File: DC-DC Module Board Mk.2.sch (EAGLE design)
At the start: 151 parts, among them Q1 FDN340P, U2 AP1117_LIN_REG, U3 LM1085IS-5.0

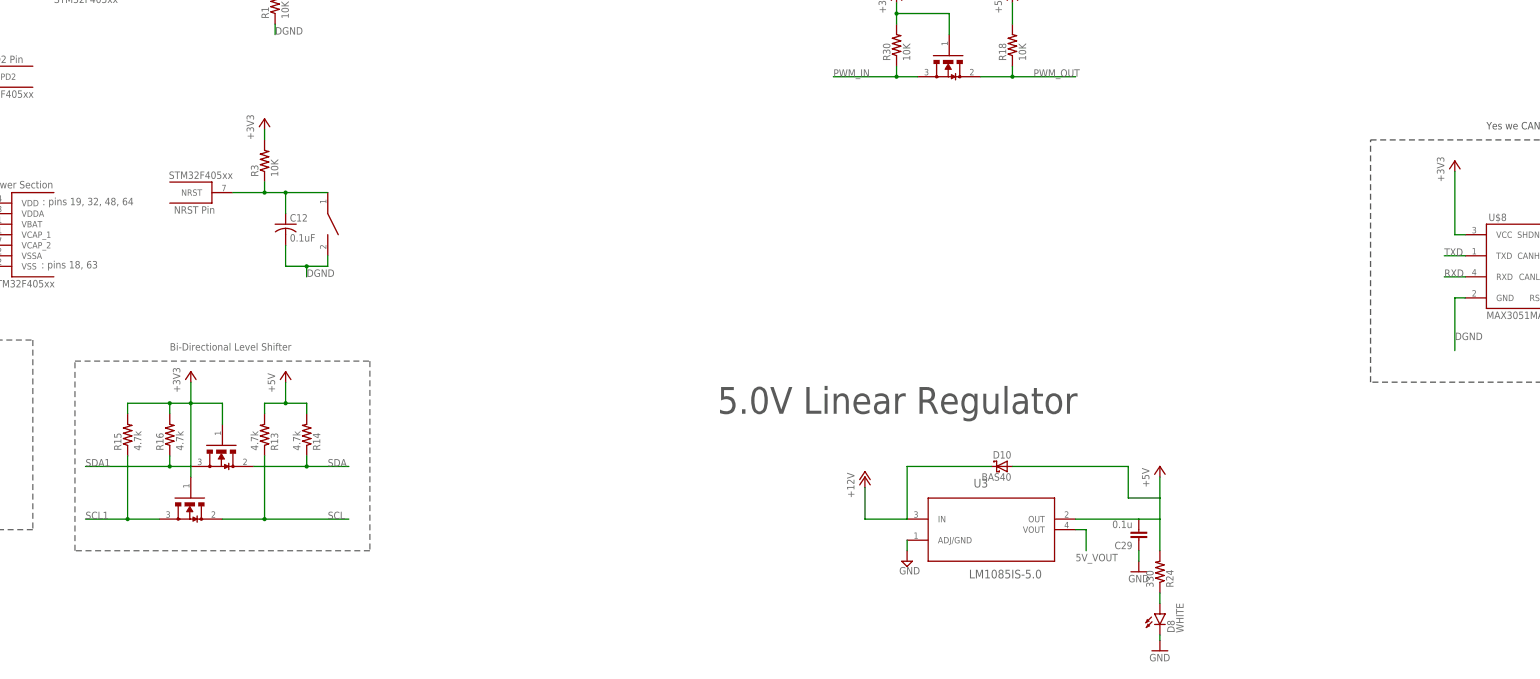
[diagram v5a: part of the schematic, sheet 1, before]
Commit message: Added header pins for debugging
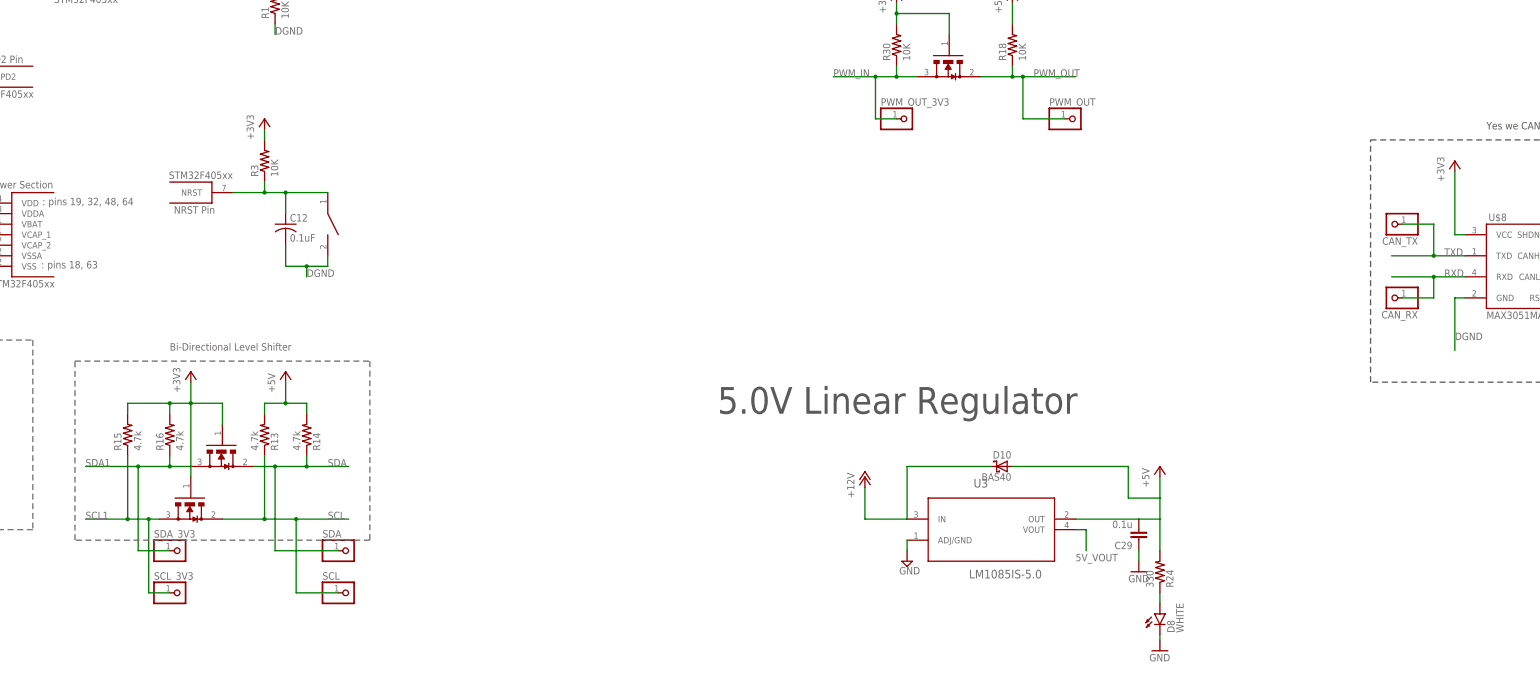
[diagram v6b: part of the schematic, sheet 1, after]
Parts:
- added CAN_RX, CAN_TX, PWM_OUT, PWM_OUT_3V3, SCL, SCL_3V3, SDA, SDA_3V3: (no value), pinhead:PINHD-1X1
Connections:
- net PWM_IN: now also PWM_OUT_3V3.1
- net PWM_OUT: now also PWM_OUT.1
- net RXD: now also CAN_RX.1
- net SCL: now also SCL.1
- net SCL1: now also SCL_3V3.1
- net SDA: now also SDA.1
- net SDA1: now also SDA_3V3.1
- net TXD: now also CAN_TX.1
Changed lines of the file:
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@@
 <?xml version="1.0" encoding="utf-8"?>
 <!DOCTYPE eagle SYSTEM "eagle.dtd">
-<eagle version="7.4.0">
+<eagle version="7.5.0">
 <drawing>
 <settings>
@@
 <part name="+3V7" library="supply1" deviceset="+3V3" device=""/>
 <part name="P+1" library="supply1" deviceset="+5V" device=""/>
+<part name="PWM_OUT_3V3" library="pinhead" deviceset="PINHD-1X1" device=""/>
+<part name="PWM_OUT" library="pinhead" deviceset="PINHD-1X1" device=""/>
+<part name="SDA_3V3" library="pinhead" deviceset="PINHD-1X1" device=""/>
+<part name="SCL_3V3" library="pinhead" deviceset="PINHD-1X1" device=""/>
+<part name="SDA" library="pinhead" deviceset="PINHD-1X1" device=""/>
+<part name="SCL" library="pinhead" deviceset="PINHD-1X1" device=""/>
+<part name="CAN_TX" library="pinhead" deviceset="PINHD-1X1" device=""/>
+<part name="CAN_RX" library="pinhead" deviceset="PINHD-1X1" device=""/>
 </parts>
 <sheets>
@@
 <wire x1="459.74" y1="-127" x2="459.74" y2="-68.58" width="0.1524" layer="97" style="shortdash"/>
 <text x="487.68" y="-66.04" size="1.778" layer="97">Yes we CAN!</text>
-<wire x1="218.44" y1="-167.64" x2="147.32" y2="-167.64" width="0.1524" layer="95" style="shortdash"/>
-<wire x1="147.32" y1="-167.64" x2="147.32" y2="-121.92" width="0.1524" layer="95" style="shortdash"/>
+<wire x1="218.44" y1="-165.1" x2="147.32" y2="-165.1" width="0.1524" layer="95" style="shortdash"/>
+<wire x1="147.32" y1="-165.1" x2="147.32" y2="-121.92" width="0.1524" layer="95" style="shortdash"/>
 <wire x1="147.32" y1="-121.92" x2="218.44" y2="-121.92" width="0.1524" layer="95" style="shortdash"/>
-<wire x1="218.44" y1="-121.92" x2="218.44" y2="-167.64" width="0.1524" layer="95" style="shortdash"/>
+<wire x1="218.44" y1="-121.92" x2="218.44" y2="-165.1" width="0.1524" layer="95" style="shortdash"/>
 <text x="170.18" y="-119.38" size="1.778" layer="95">Bi-Directional Level Shifter</text>
 <text x="12.7" y="208.28" size="5.08" layer="97">Brick 1</text>
@@
 <instance part="+3V7" gate="G$1" x="345.44" y="-33.02"/>
 <instance part="P+1" gate="1" x="373.38" y="-33.02"/>
+<instance part="PWM_OUT_3V3" gate="G$1" x="347.98" y="-63.5"/>
+<instance part="PWM_OUT" gate="G$1" x="388.62" y="-63.5"/>
+<instance part="SDA_3V3" gate="G$1" x="172.72" y="-167.64"/>
+<instance part="SCL_3V3" gate="G$1" x="172.72" y="-177.8"/>
+<instance part="SDA" gate="G$1" x="213.36" y="-167.64"/>
+<instance part="SCL" gate="G$1" x="213.36" y="-177.8"/>
+<instance part="CAN_TX" gate="G$1" x="464.82" y="-88.9" rot="R180"/>
+<instance part="CAN_RX" gate="G$1" x="464.82" y="-106.68" rot="R180"/>
 </instances>
 <busses>
@@
 <wire x1="182.88" y1="-160.02" x2="193.04" y2="-160.02" width="0.1524" layer="91"/>
 <pinref part="R13" gate="G$1" pin="1"/>
-<wire x1="193.04" y1="-160.02" x2="213.36" y2="-160.02" width="0.1524" layer="91"/>
+<wire x1="193.04" y1="-160.02" x2="200.66" y2="-160.02" width="0.1524" layer="91"/>
+<wire x1="200.66" y1="-160.02" x2="213.36" y2="-160.02" width="0.1524" layer="91"/>
 <wire x1="193.04" y1="-144.78" x2="193.04" y2="-160.02" width="0.1524" layer="91"/>
 <junction x="193.04" y="-160.02"/>
 <label x="208.28" y="-160.02" size="1.778" layer="95"/>
+<pinref part="SCL" gate="G$1" pin="1"/>
+<wire x1="200.66" y1="-177.8" x2="210.82" y2="-177.8" width="0.1524" layer="91"/>
+<wire x1="200.66" y1="-177.8" x2="200.66" y2="-160.02" width="0.1524" layer="91"/>
+<junction x="200.66" y="-160.02"/>
 </segment>
 <segment>
@@
 <segment>
 <pinref part="U$9" gate="G$1" pin="D"/>
-<wire x1="190.5" y1="-147.32" x2="203.2" y2="-147.32" width="0.1524" layer="91"/>
+<wire x1="190.5" y1="-147.32" x2="195.58" y2="-147.32" width="0.1524" layer="91"/>
 <pinref part="R14" gate="G$1" pin="1"/>
+<wire x1="195.58" y1="-147.32" x2="203.2" y2="-147.32" width="0.1524" layer="91"/>
 <wire x1="203.2" y1="-147.32" x2="213.36" y2="-147.32" width="0.1524" layer="91"/>
 <wire x1="203.2" y1="-144.78" x2="203.2" y2="-147.32" width="0.1524" layer="91"/>
 <junction x="203.2" y="-147.32"/>
 <label x="208.28" y="-147.32" size="1.778" layer="95"/>
+<wire x1="195.58" y1="-147.32" x2="195.58" y2="-167.64" width="0.1524" layer="91"/>
+<junction x="195.58" y="-147.32"/>
+<pinref part="SDA" gate="G$1" pin="1"/>
+<wire x1="195.58" y1="-167.64" x2="210.82" y2="-167.64" width="0.1524" layer="91"/>
 </segment>
 <segment>
@@
 <segment>
 <pinref part="U$8" gate="G$1" pin="TXD"/>
-<wire x1="482.6" y1="-96.52" x2="477.52" y2="-96.52" width="0.1524" layer="91"/>
 <label x="477.52" y="-96.52" size="1.778" layer="95"/>
+<wire x1="482.6" y1="-96.52" x2="474.98" y2="-96.52" width="0.1524" layer="91"/>
+<wire x1="474.98" y1="-96.52" x2="464.82" y2="-96.52" width="0.1524" layer="91"/>
+<wire x1="474.98" y1="-96.52" x2="474.98" y2="-88.9" width="0.1524" layer="91"/>
+<junction x="474.98" y="-96.52"/>
+<pinref part="CAN_TX" gate="G$1" pin="1"/>
+<wire x1="474.98" y1="-88.9" x2="467.36" y2="-88.9" width="0.1524" layer="91"/>
 </segment>
 <segment>
@@
 <segment>
 <pinref part="U$8" gate="G$1" pin="RXD"/>
-<wire x1="482.6" y1="-101.6" x2="477.52" y2="-101.6" width="0.1524" layer="91"/>
 <label x="477.52" y="-101.6" size="1.778" layer="95"/>
+<wire x1="482.6" y1="-101.6" x2="474.98" y2="-101.6" width="0.1524" layer="91"/>
+<wire x1="474.98" y1="-101.6" x2="464.82" y2="-101.6" width="0.1524" layer="91"/>
+<wire x1="474.98" y1="-101.6" x2="474.98" y2="-106.68" width="0.1524" layer="91"/>
+<junction x="474.98" y="-101.6"/>
+<pinref part="CAN_RX" gate="G$1" pin="1"/>
+<wire x1="474.98" y1="-106.68" x2="467.36" y2="-106.68" width="0.1524" layer="91"/>
 </segment>
 <segment>
@@
 <wire x1="175.26" y1="-147.32" x2="170.18" y2="-147.32" width="0.1524" layer="91"/>
 <pinref part="R16" gate="G$1" pin="1"/>
-<wire x1="170.18" y1="-147.32" x2="149.86" y2="-147.32" width="0.1524" layer="91"/>
+<wire x1="170.18" y1="-147.32" x2="162.56" y2="-147.32" width="0.1524" layer="91"/>
+<wire x1="162.56" y1="-147.32" x2="149.86" y2="-147.32" width="0.1524" layer="91"/>
 <wire x1="170.18" y1="-147.32" x2="170.18" y2="-144.78" width="0.1524" layer="91"/>
 <junction x="170.18" y="-147.32"/>
 <label x="149.86" y="-147.32" size="1.778" layer="95"/>
+<wire x1="162.56" y1="-147.32" x2="162.56" y2="-167.64" width="0.1524" layer="91"/>
+<junction x="162.56" y="-147.32"/>
+<pinref part="SDA_3V3" gate="G$1" pin="1"/>
+<wire x1="162.56" y1="-167.64" x2="170.18" y2="-167.64" width="0.1524" layer="91"/>
 </segment>
 <segment>
@@
 <segment>
 <pinref part="BSS138" gate="G$1" pin="S"/>
-<wire x1="167.64" y1="-160.02" x2="160.02" y2="-160.02" width="0.1524" layer="91"/>
+<wire x1="167.64" y1="-160.02" x2="165.1" y2="-160.02" width="0.1524" layer="91"/>
 <pinref part="R15" gate="G$1" pin="1"/>
+<wire x1="165.1" y1="-160.02" x2="160.02" y2="-160.02" width="0.1524" layer="91"/>
 <wire x1="160.02" y1="-160.02" x2="149.86" y2="-160.02" width="0.1524" layer="91"/>
 <wire x1="160.02" y1="-144.78" x2="160.02" y2="-160.02" width="0.1524" layer="91"/>
 <junction x="160.02" y="-160.02"/>
 <label x="149.86" y="-160.02" size="1.778" layer="95"/>
+<wire x1="165.1" y1="-160.02" x2="165.1" y2="-177.8" width="0.1524" layer="91"/>
+<junction x="165.1" y="-160.02"/>
+<pinref part="SCL_3V3" gate="G$1" pin="1"/>
+<wire x1="165.1" y1="-177.8" x2="170.18" y2="-177.8" width="0.1524" layer="91"/>
 </segment>
 <segment>
@@
 <segment>
 <pinref part="R18" gate="G$1" pin="1"/>
-<wire x1="373.38" y1="-53.34" x2="388.62" y2="-53.34" width="0.1524" layer="91"/>
+<wire x1="373.38" y1="-53.34" x2="375.92" y2="-53.34" width="0.1524" layer="91"/>
+<wire x1="375.92" y1="-53.34" x2="388.62" y2="-53.34" width="0.1524" layer="91"/>
 <wire x1="373.38" y1="-50.8" x2="373.38" y2="-53.34" width="0.1524" layer="91"/>
 <pinref part="U$12" gate="G$1" pin="D"/>
@@
 <junction x="373.38" y="-53.34"/>
 <label x="378.46" y="-53.34" size="1.778" layer="95"/>
+<wire x1="375.92" y1="-53.34" x2="375.92" y2="-63.5" width="0.1524" layer="91"/>
+<junction x="375.92" y="-53.34"/>
+<pinref part="PWM_OUT" gate="G$1" pin="1"/>
+<wire x1="375.92" y1="-63.5" x2="386.08" y2="-63.5" width="0.1524" layer="91"/>
 </segment>
 <segment>
@@
 <pinref part="U$12" gate="G$1" pin="S"/>
 <pinref part="R30" gate="G$1" pin="1"/>
-<wire x1="345.44" y1="-53.34" x2="330.2" y2="-53.34" width="0.1524" layer="91"/>
+<wire x1="345.44" y1="-53.34" x2="340.36" y2="-53.34" width="0.1524" layer="91"/>
+<wire x1="340.36" y1="-53.34" x2="330.2" y2="-53.34" width="0.1524" layer="91"/>
 <wire x1="345.44" y1="-50.8" x2="345.44" y2="-53.34" width="0.1524" layer="91"/>
 <junction x="345.44" y="-53.34"/>
 <label x="330.2" y="-53.34" size="1.778" layer="95"/>
-</segment>
-<segment>
+<wire x1="340.36" y1="-53.34" x2="340.36" y2="-63.5" width="0.1524" layer="91"/>
+<junction x="340.36" y="-53.34"/>
+<pinref part="PWM_OUT_3V3" gate="G$1" pin="1"/>
+<wire x1="340.36" y1="-63.5" x2="345.44" y2="-63.5" width="0.1524" layer="91"/>
+</segment>
+<segment>

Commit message: moved sda/scl pins and header pins
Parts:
- removed D8: WHITE, SparkFun-LED:LED-WHITE1206
- added D7: RED, SparkFun-LED:LED-RED0603
- D1: value WHITE -> RED; device SparkFun-LED:LED-WHITE1206 -> SparkFun-LED:LED-RED0603
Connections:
- removed net PB10: U$5G$2.PB10
- removed net PB11: U$5G$2.PB11
- new net PB7: U$5G$2.PB7
- new net PB8: U$5G$2.PB8
- net GND: now also D7.C; no longer D8.C
- net N$22: now also D7.A; no longer D8.A
- net SCL1: now also U$5G$2.PB10; no longer U$5G$2.PB8
- net SDA1: now also U$5G$2.PB11; no longer U$5G$2.PB7
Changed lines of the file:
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@@
 <?xml version="1.0" encoding="utf-8"?>
 <!DOCTYPE eagle SYSTEM "eagle.dtd">
-<eagle version="7.5.0">
+<eagle version="7.4.0">
 <drawing>
 <settings>
@@
 <part name="U$18" library="Connectors" deviceset="XT60" device=""/>
 <part name="U$19" library="Connectors" deviceset="XT60" device=""/>
-<part name="D8" library="SparkFun-LED" deviceset="LED-WHITE" device="1206" value="WHITE"/>
 <part name="R24" library="resistor" deviceset="R-US_" device="R0603" value="330"/>
-<part name="SUPPLY18" library="supply1" deviceset="GND" device=""/>
 <part name="U3" library="NSC_By_element14_Batch_1" deviceset="LM1085IS-5.0" device=""/>
 <part name="5V_GND" library="supply2" deviceset="GND" device=""/>
@@
 <part name="P+9" library="supply1" deviceset="+12V" device=""/>
 <part name="R21" library="resistor" deviceset="R-US_" device="R0603" value="200"/>
-<part name="D1" library="SparkFun-LED" deviceset="LED-WHITE" device="1206" value="WHITE"/>
 <part name="GND7" library="SparkFun-Aesthetics" deviceset="GND" device=""/>
 <part name="U$21" library="Connectors" deviceset="XT60" device=""/>
@@
 <part name="CAN_TX" library="pinhead" deviceset="PINHD-1X1" device=""/>
 <part name="CAN_RX" library="pinhead" deviceset="PINHD-1X1" device=""/>
+<part name="D7" library="SparkFun-LED" deviceset="LED-RED" device="0603" value="RED"/>
+<part name="GND9" library="SparkFun-Aesthetics" deviceset="GND" device=""/>
+<part name="D1" library="SparkFun-LED" deviceset="LED-RED" device="0603" value="RED"/>
 </parts>
 <sheets>
@@
 <instance part="U$18" gate="G$1" x="381" y="88.9" rot="R180"/>
 <instance part="U$19" gate="G$1" x="381" y="71.12" rot="R180"/>
-<instance part="D8" gate="G$1" x="408.94" y="-182.88"/>
 <instance part="R24" gate="G$1" x="408.94" y="-172.72" rot="MR90"/>
-<instance part="SUPPLY18" gate="1" x="408.94" y="-191.77"/>
 <instance part="U3" gate="A" x="368.3" y="-160.02"/>
 <instance part="5V_GND" gate="GND" x="347.98" y="-170.18"/>
@@
 <instance part="P+9" gate="1" x="337.82" y="-149.86"/>
 <instance part="R21" gate="G$1" x="109.22" y="-137.16" rot="MR0"/>
-<instance part="D1" gate="G$1" x="114.3" y="-144.78"/>
 <instance part="GND7" gate="1" x="114.3" y="-154.94" smashed="yes">
 <attribute name="VALUE" x="111.76" y="-157.48" size="1.778" layer="96"/>
@@
 <instance part="CAN_TX" gate="G$1" x="464.82" y="-88.9" rot="R180"/>
 <instance part="CAN_RX" gate="G$1" x="464.82" y="-106.68" rot="R180"/>
+<instance part="D7" gate="G$1" x="408.94" y="-182.88"/>
+<instance part="GND9" gate="1" x="408.94" y="-195.58" smashed="yes">
+<attribute name="VALUE" x="406.4" y="-198.12" size="1.778" layer="96"/>
+</instance>
+<instance part="D1" gate="G$1" x="114.3" y="-144.78"/>
 </instances>
 <busses>
@@
 </segment>
 <segment>
-<pinref part="D8" gate="G$1" pin="C"/>
-<pinref part="SUPPLY18" gate="1" pin="GND"/>
-<wire x1="408.94" y1="-187.96" x2="408.94" y2="-189.23" width="0.1524" layer="91"/>
-</segment>
-<segment>
 <pinref part="U3" gate="A" pin="ADJ/GND"/>
 <pinref part="5V_GND" gate="GND" pin="GND"/>
@@
 </segment>
 <segment>
-<pinref part="D1" gate="G$1" pin="C"/>
 <pinref part="GND7" gate="1" pin="GND"/>
 <wire x1="114.3" y1="-149.86" x2="114.3" y2="-152.4" width="0.1524" layer="91"/>
+<pinref part="D1" gate="G$1" pin="C"/>
 </segment>
 <segment>
@@
 <wire x1="436.88" y1="180.34" x2="441.96" y2="180.34" width="0.1524" layer="91"/>
 <label x="441.96" y="180.34" size="1.27" layer="95" xref="yes"/>
+</segment>
+<segment>
+<pinref part="D7" gate="G$1" pin="C"/>
+<wire x1="408.94" y1="-187.96" x2="408.94" y2="-193.04" width="0.1524" layer="91"/>
+<pinref part="GND9" gate="1" pin="GND"/>
 </segment>
 </net>
@@
 </segment>
 <segment>
-<pinref part="U$5" gate="G$2" pin="PB7"/>
-<wire x1="45.72" y1="-35.56" x2="40.64" y2="-35.56" width="0.1524" layer="91"/>
-<label x="38.1" y="-35.56" size="1.778" layer="95"/>
+<pinref part="U$5" gate="G$2" pin="PB11"/>
+<wire x1="45.72" y1="-45.72" x2="40.64" y2="-45.72" width="0.1524" layer="91"/>
+<label x="38.1" y="-45.72" size="1.778" layer="95"/>
 </segment>
 </net>
@@
 </segment>
 <segment>
-<pinref part="U$5" gate="G$2" pin="PB8"/>
-<wire x1="45.72" y1="-38.1" x2="40.64" y2="-38.1" width="0.1524" layer="91"/>
-<label x="38.1" y="-38.1" size="1.778" layer="95"/>
+<pinref part="U$5" gate="G$2" pin="PB10"/>
+<wire x1="45.72" y1="-43.18" x2="40.64" y2="-43.18" width="0.1524" layer="91"/>
+<label x="38.1" y="-43.18" size="1.778" layer="95"/>
 </segment>
 </net>
@@
 <net name="N$22" class="0">
 <segment>
-<pinref part="D8" gate="G$1" pin="A"/>
 <pinref part="R24" gate="G$1" pin="1"/>
 <wire x1="408.94" y1="-177.8" x2="408.94" y2="-180.34" width="0.1524" layer="91"/>
+<pinref part="D7" gate="G$1" pin="A"/>
 </segment>
 </net>
@@
 <wire x1="391.16" y1="-162.56" x2="391.16" y2="-167.64" width="0.1524" layer="91"/>
 <label x="388.62" y="-170.18" size="1.778" layer="95"/>
-</segment>
-</net>
-<net name="N$5" class="0">
-<segment>
-<pinref part="R21" gate="G$1" pin="1"/>
-<pinref part="D1" gate="G$1" pin="A"/>
-<wire x1="114.3" y1="-137.16" x2="114.3" y2="-142.24" width="0.1524" layer="91"/>
 </segment>
 </net>
@@
 </segment>
 </net>
-<net name="PB10" class="0">
-<segment>
-<pinref part="U$5" gate="G$2" pin="PB10"/>
-<wire x1="45.72" y1="-43.18" x2="40.64" y2="-43.18" width="0.1524" layer="91"/>
-<label x="38.1" y="-43.18" size="1.778" layer="95"/>
-</segment>
-</net>
-<net name="PB11" class="0">
-<segment>
-<pinref part="U$5" gate="G$2" pin="PB11"/>
-<wire x1="45.72" y1="-45.72" x2="40.64" y2="-45.72" width="0.1524" layer="91"/>
-<label x="38.1" y="-45.72" size="1.778" layer="95"/>
-</segment>
-</net>
+<net name="PB7" class="0">
+<segment>
+<pinref part="U$5" gate="G$2" pin="PB7"/>
+<wire x1="45.72" y1="-35.56" x2="40.64" y2="-35.56" width="0.1524" layer="91"/>
+<label x="38.1" y="-35.56" size="1.778" layer="95"/>
+</segment>
+</net>
+<net name="PB8" class="0">
+<segment>
+<pinref part="U$5" gate="G$2" pin="PB8"/>
+<wire x1="45.72" y1="-38.1" x2="40.64" y2="-38.1" width="0.1524" layer="91"/>
+<label x="38.1" y="-38.1" size="1.778" layer="95"/>
+</segment>
+</net>
+<net name="N$5" class="0">
+<segment>
+<pinref part="R21" gate="G$1" pin="1"/>
+<pinref part="D1" gate="G$1" pin="A"/>
+<wire x1="114.3" y1="-137.16" x2="114.3" y2="-142.24" width="0.1524" layer="91"/>
+</segment>
+</net>
